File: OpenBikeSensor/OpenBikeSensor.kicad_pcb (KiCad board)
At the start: 2 copper layers, 64.5 x 65.2 mm, 33 parts, among them J1 Battery, J2 On/Off, J3 Display Cable, J4 Add-ons, M1 ESP32 WROOM 30-Pin, M2 LIPoChargerwithProtection, M3 DCDC_fix, M4 SD, M5 GPS

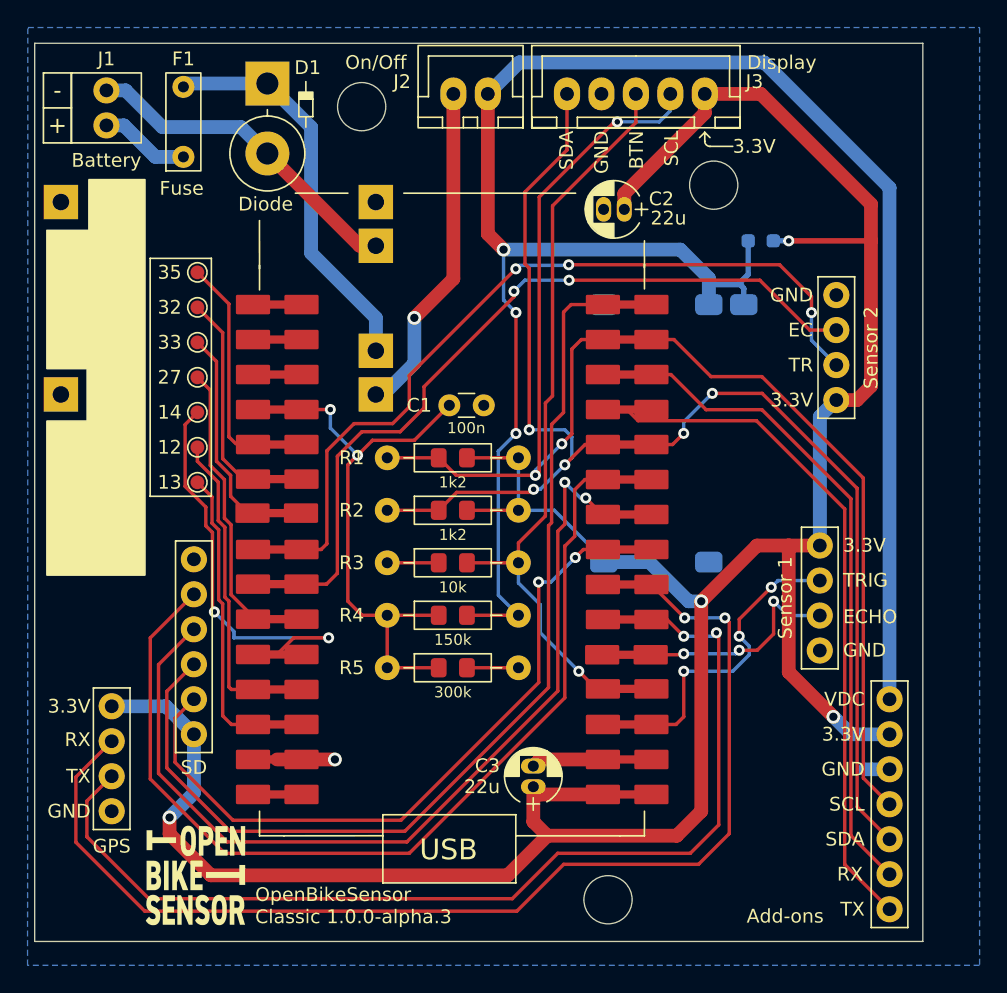
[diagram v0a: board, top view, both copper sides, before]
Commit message: 0603 instead of 0805
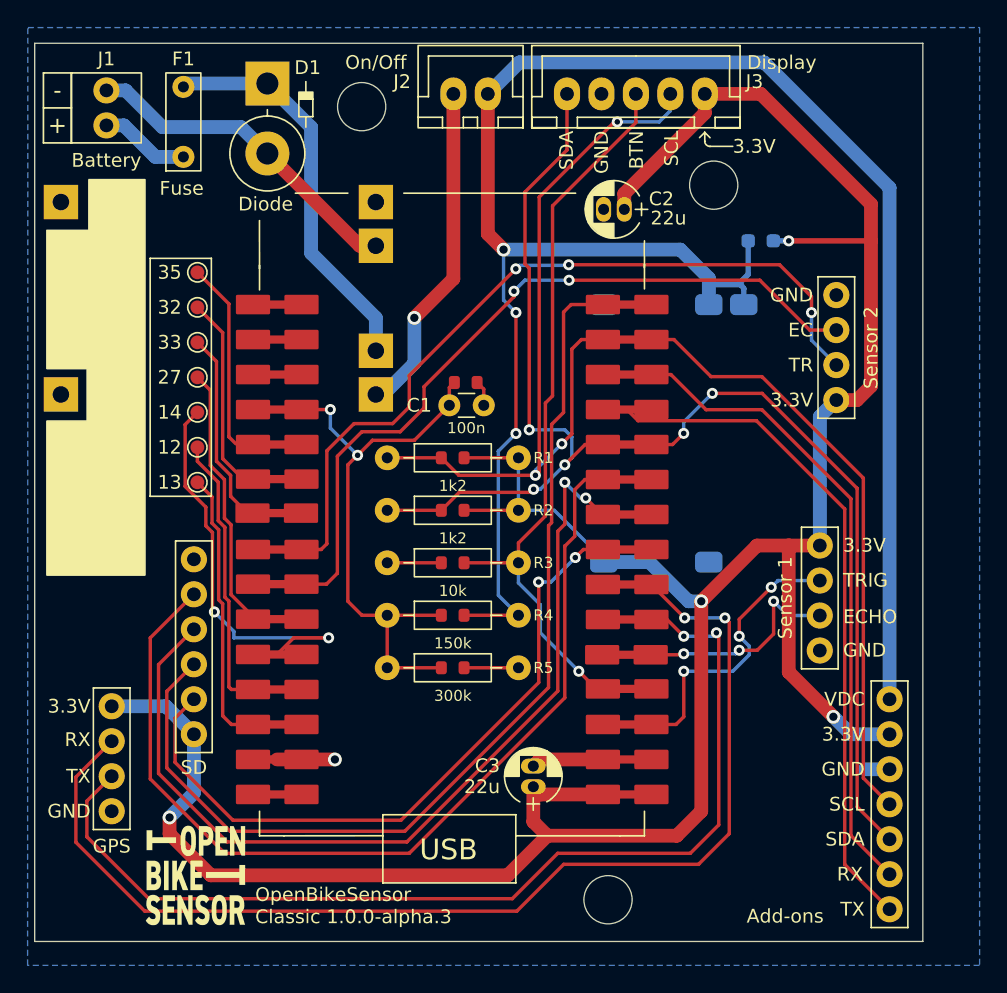
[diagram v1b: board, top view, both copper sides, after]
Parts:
- C1: footprint Capacitors_THT:C_Disc_D3.0mm_W1.6mm_P2.50mm -> OpenBikeSensor:C_Disc_D3.0mm_W1.6mm_P2.50mm_0603
- R1, R2, R3, R4, R5: footprint OpenBikeSensor:Resistor_Combined_THT3_SMD0805 -> OpenBikeSensor:Resistor_Combined_THT3_SMD0603
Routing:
- net GND: track 18.8 -> 21.0 mm
- net /V_MEA: track 41.6 -> 43.8 mm

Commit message: natenom träne
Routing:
- net /IO14: track 29.3 -> 22.6 mm
- net GND: track 21.0 -> 16.8 mm, vias 1 -> 95
- net SDA: track 98.7 -> 96.6 mm
- net +3.3V: track 198.0 -> 199.0 mm
- net SD_CMD: track 74.8 -> 74.3 mm
- added copper zone on F.Cu, net GND
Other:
- outline, holes or cut-outs redrawn
- board text removed: "OpenBikeSensor Rev ${REVISION}"
